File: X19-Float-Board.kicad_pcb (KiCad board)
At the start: 2 copper layers, 83.1 x 86.2 mm, 31 parts, among them J1 USB4220-03-1040-C_REVA, SW2 SW_Nidec_CAS-120A1, U3 STM32G431RBT6

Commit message: Checkpoint
Checkpoint, pre battery telemetry, pre new stm
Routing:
- net /Motor/Motor PWM: track 1.65 -> 45.1 mm, vias 0 -> 4
- net GND: track 200.7 -> 241.5 mm, vias 4 -> 6
- net VBUS_A: track 31.0 -> 38.1 mm, vias 5 -> 4
- net VBUS_B: track 3.12 -> 4.71 mm
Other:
- board text added: "yo"

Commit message: Update
Update
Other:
- board size 83.1 x 86.2 mm -> 86 x 86 mm

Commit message: todolist update
update of the to do list on schematic
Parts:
- added C_D_STM2: 100nF, Capacitor_SMD:C_0603_1608Metric, F.Cu at (177.0, 51.4)
- added C_D_STM3: 100nF, Capacitor_SMD:C_0603_1608Metric, F.Cu at (177.0, 53.9)
- added R_PD_USBC_1: 5.1k, Resistor_SMD:R_0603_1608Metric, F.Cu at (183.0, 51.4)
- added R_PD_USBC_2: 5.1kΩ, Resistor_SMD:R_0603_1608Metric, F.Cu at (183.0, 53.9)
- added R_USBC_DIV1: 20kΩ, Resistor_SMD:R_0603_1608Metric, F.Cu at (183.0, 56.4)
- added R_USBC_DIV2: 10kΩ, Resistor_SMD:R_0603_1608Metric, F.Cu at (183.0, 58.9)
- added U2: STM32C542CCT6, rov_logic:LQFP48-7X7, F.Cu at (169.2, 56.0)
- added U4: INA228AIDGSR, CustomFootprints:VSSOP10_DGS_TEX, F.Cu at (167.0, 66.2)
- added U5: TPS561208DDCR, CustomFootprints:DDC0006A_N, F.Cu at (175.6, 66.1)
- added U6: TMP1075NDRLR, CustomFootprints:SOT5X3-6_DRL_TEX, F.Cu at (165.7, 70.2)
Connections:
- DEPTH_CONN1 pad 2: /sensor/Depth SCL -> /Sensors/Depth SCL
- DEPTH_CONN1 pad 3: /sensor/Depth SDA -> /Sensors/Depth SDA
- R_PU_DEPTH_0 pad 1: /sensor/Depth SCL -> /Sensors/Depth SCL
- R_PU_DEPTH_1 pad 1: /sensor/Depth SDA -> /Sensors/Depth SDA

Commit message: footprints
footprints
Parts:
- removed BUCK_12_3.3: LM2596S-3.3, Package_TO_SOT_SMD:TO-263-5_TabPin3
- removed C_D_DEPTH1, C_D_MOTOR1, C_D_RF1, C_D_STM1, C_D_STM2, C_D_STM3, C_D_SWITCH1: 100nF, Capacitor_SMD:C_0603_1608Metric
- removed C_D_PWR_0: 680µF, Capacitor_SMD:C_0603_1608Metric
- removed C_D_PWR_1: 220µF, Capacitor_SMD:C_0603_1608Metric
- removed C_D_PWR_12, C_D_PWR_3.3: 4.7µF, Capacitor_SMD:C_0603_1608Metric
- removed D1: D_MOTOR, Diode_SMD:D_SOD-123
- removed DEPTH_CONN1: Conn_01x04_Pin, Connector_JST:JST_GH_BM04B-GHS-TBT_1x04-1MP_P1.25mm_Vertical
- removed D_PWR1: 1N5822, Diode_THT:D_DO-201AD_P15.24mm_Horizontal
- removed FUSE_PWR1: 2A 12V PTC fuse, Fuse:Fuse_1812_4532Metric
- removed J1: USB4220-03-1040-C_REVA, usbc:GCT_USB4220-03-1040-C_REVA
- removed L_PWR1: 33µH, Inductor_SMD:L_0603_1608Metric
- removed MOTOR_CONN1: Motor, TerminalBlock_Phoenix:TerminalBlock_Phoenix_MKDS-1,5-2-5.08_1x02_P5.08mm_Horizontal
- removed NMOS_MOTOR1: NMOS, Package_TO_SOT_SMD:SOT-23_Handsoldering
- removed R_PD_MOTOR1, R_PU_SWITCH1: 10kΩ, Resistor_SMD:R_0603_1608Metric
- removed R_PD_USBC_1 (x2): 5.1k, Resistor_SMD:R_0603_1608Metric
- removed R_PD_USBC_2 (x2): 5.1kΩ, Resistor_SMD:R_0603_1608Metric
- removed R_PU_DEPTH_0, R_PU_DEPTH_1: 4.7kΩ, Resistor_SMD:R_0603_1608Metric
- removed R_PWM_MOTOR1: 220Ω, Resistor_SMD:R_0603_1608Metric
- removed R_USBC_DIV0, R_USBC_DIV1: 20kΩ, Resistor_SMD:R_0603_1608Metric
- removed R_USBC_DIV1, R_USBC_DIV2: 10kΩ, Resistor_SMD:R_0603_1608Metric
- removed SCREW_PWR1: Screw_Terminal_01x02, TerminalBlock_Phoenix:TerminalBlock_Phoenix_MKDS-1,5-2-5.08_1x02_P5.08mm_Horizontal
- removed SW2: SW_Nidec_CAS-120A1, Button_Switch_SMD:Nidec_Copal_CAS-120A
- removed U1: ~, customrf:rf module
- removed U2: STM32C542CCT6, rov_logic:LQFP48-7X7
- removed U3: STM32G431RBT6, stm32:LQFP64-10x10mm
- removed U4: INA228AIDGSR, CustomFootprints:VSSOP10_DGS_TEX
- removed U5: TPS561208DDCR, CustomFootprints:DDC0006A_N
- removed U6: TMP1075NDRLR, CustomFootprints:SOT5X3-6_DRL_TEX
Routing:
- net GND: track 241.5 -> 0.00 mm, vias 6 -> 0
- net 3.3 V: track 149.3 -> 0.00 mm, vias 3 -> 0
- net 12 V: track 80.6 -> 0.00 mm, vias 2 -> 0
- net /rf/RF RST: track 45.4 -> 0.00 mm, vias 3 -> 0
- net /Motor/Motor PWM: track 45.1 -> 0.00 mm, vias 4 -> 0
- net /rf/RF NSS: track 45.0 -> 0.00 mm, vias 1 -> 0
- net /rf/RF MOSI: track 41.9 -> 0.00 mm, vias 3 -> 0
- net /sensor/Depth SDA: track 41.1 -> 0.00 mm
- net VBUS_A: track 38.1 -> 0.00 mm, vias 4 -> 0
- net /rf/RF MISO: track 37.4 -> 0.00 mm, vias 1 -> 0
- net /rf/RF SCK: track 36.4 -> 0.00 mm, vias 1 -> 0
- net /sensor/Depth SCL: track 33.5 -> 0.00 mm, vias 2 -> 0
- net /rf/RF INT: track 30.0 -> 0.00 mm, vias 1 -> 0
- net Net-(J1-DN2): track 23.7 -> 0.00 mm
- net Net-(D1-A): track 19.5 -> 0.00 mm, vias 1 -> 0
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- removed copper zone on F.Cu, net 12 V
- removed copper zone on F.Cu, net GND
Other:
- board text removed: "yo"

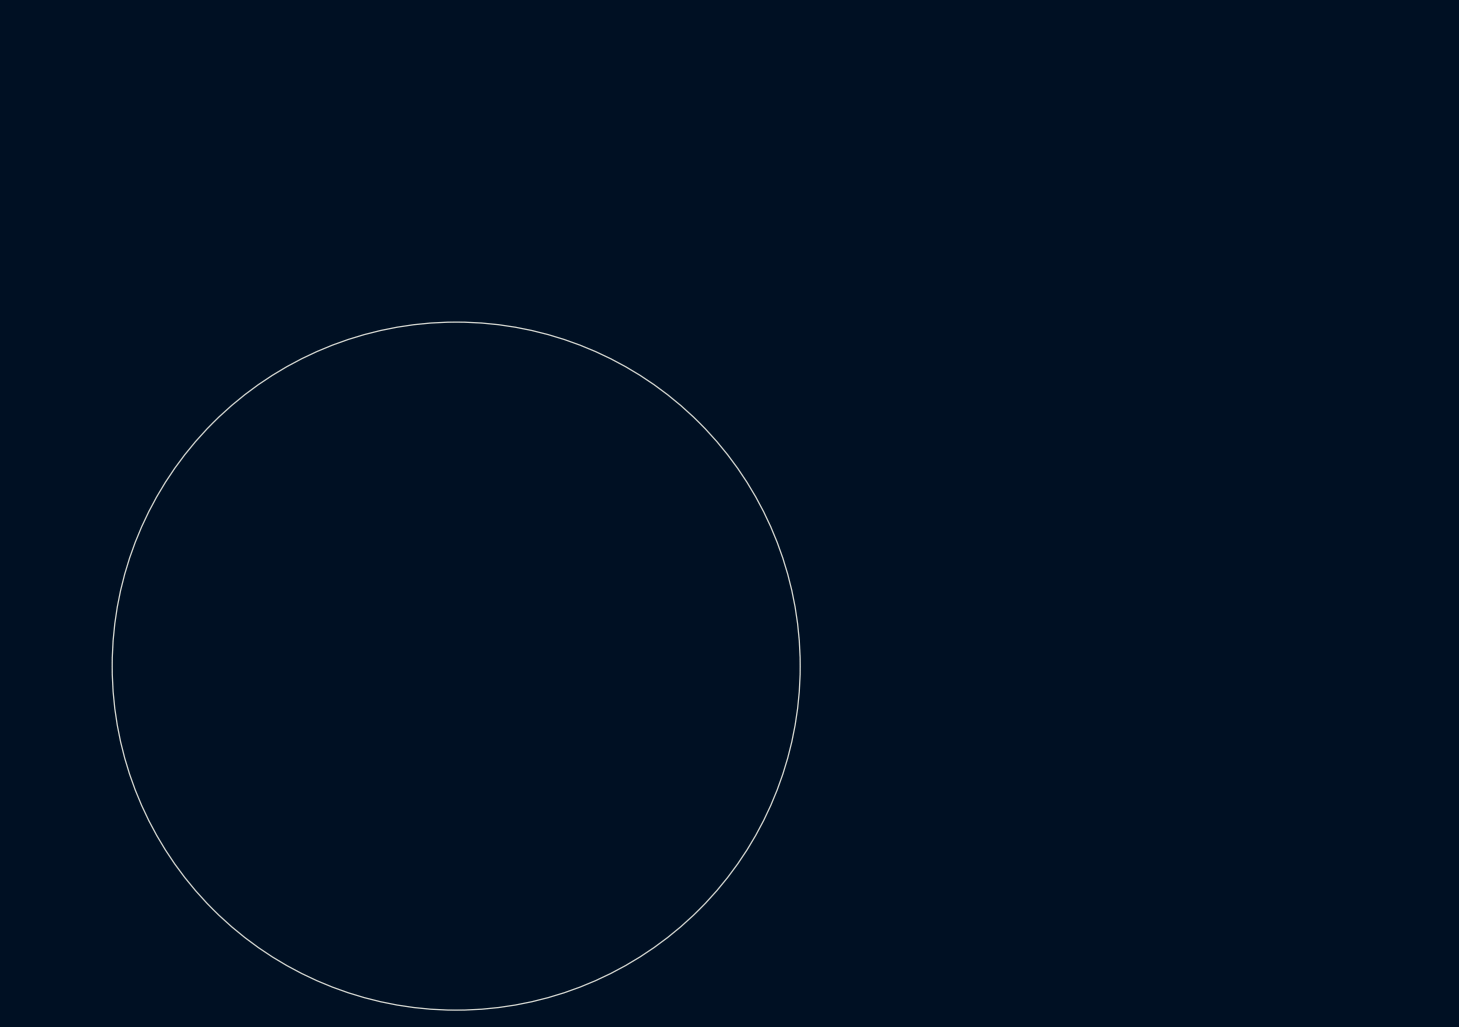
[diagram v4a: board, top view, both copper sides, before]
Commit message: Finished footprints
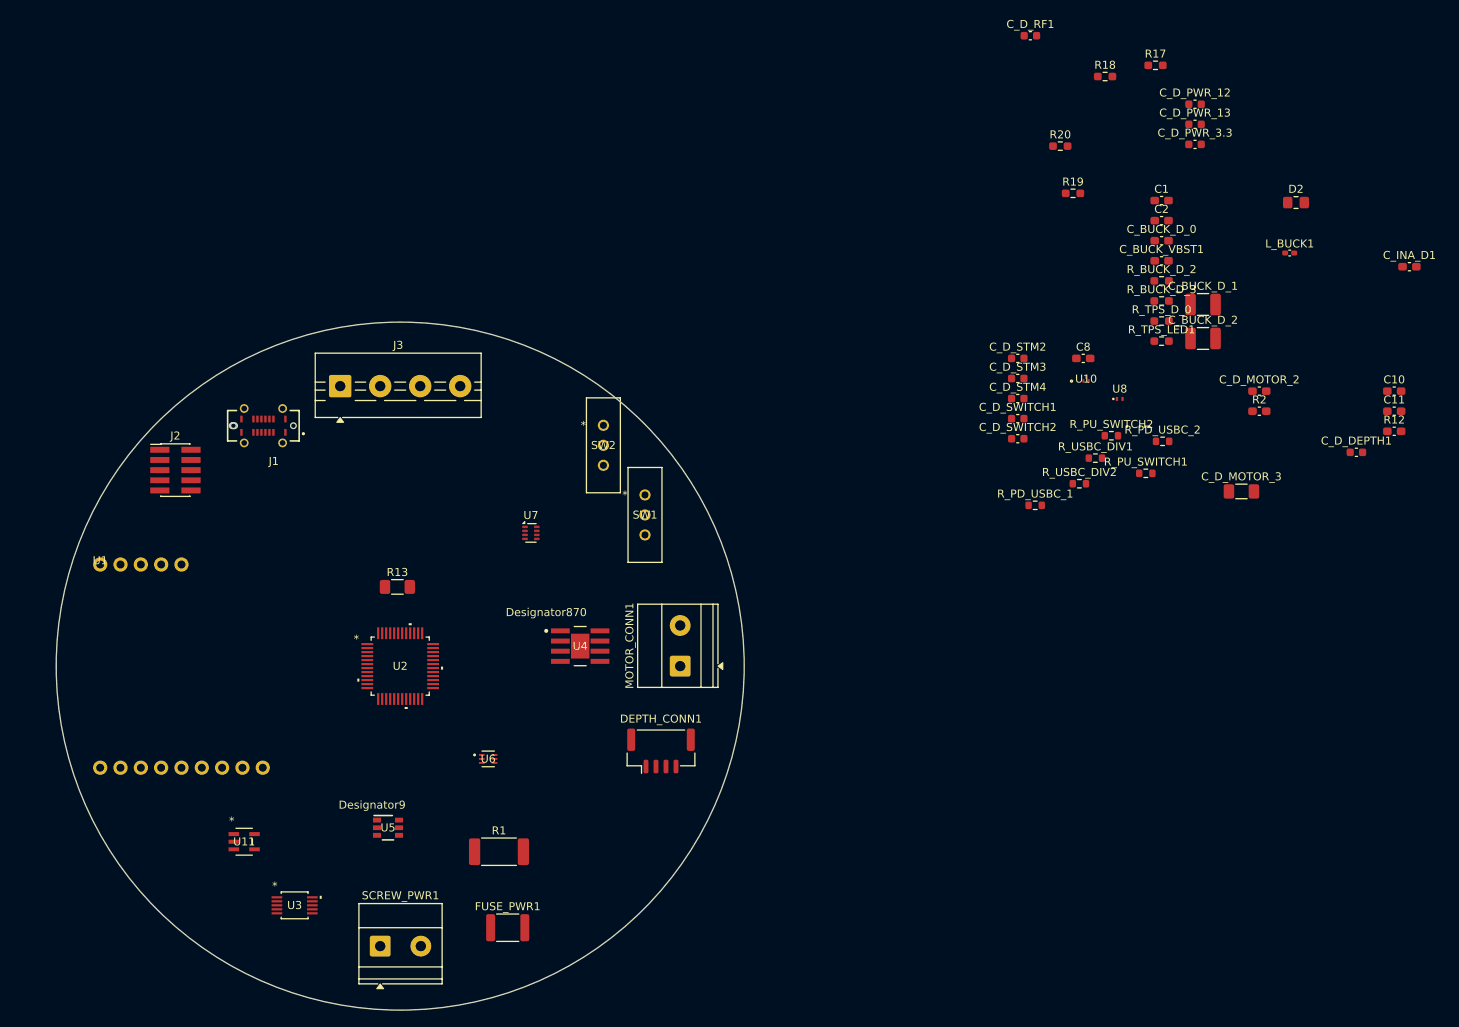
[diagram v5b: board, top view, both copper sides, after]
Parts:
- added C1: 1uF, Capacitor_SMD:C_0603_1608Metric_Pad1.08x0.95mm_HandSolder, F.Cu at (245.2, 41.8)
- added C10: 100nf, Capacitor_SMD:C_0603_1608Metric_Pad1.08x0.95mm_HandSolder, F.Cu at (274.3, 65.6)
- added C11: 10nf, Capacitor_SMD:C_0603_1608Metric_Pad1.08x0.95mm_HandSolder, F.Cu at (274.3, 68.1)
- added C2: 1uF, Capacitor_SMD:C_0603_1608Metric_Pad1.08x0.95mm_HandSolder, F.Cu at (245.2, 44.3)
- added C8: 100nf, Capacitor_SMD:C_0603_1608Metric_Pad1.08x0.95mm_HandSolder, F.Cu at (235.4, 61.5)
- added C_BUCK_D_0: .1uF, Capacitor_SMD:C_0603_1608Metric_Pad1.08x0.95mm_HandSolder, F.Cu at (245.2, 46.8)
- added C_BUCK_D_1: 22uF, Capacitor_SMD:C_1210_3225Metric_Pad1.33x2.70mm_HandSolder, F.Cu at (250.4, 54.8)
- added C_BUCK_D_2: 22uF, Capacitor_SMD:C_1210_3225Metric_Pad1.33x2.70mm_HandSolder, F.Cu at (250.4, 59.0)
- added C_BUCK_VBST1: 0.1 uF, Capacitor_SMD:C_0603_1608Metric_Pad1.08x0.95mm_HandSolder, F.Cu at (245.2, 49.3)
- added C_D_DEPTH1: 100nF, Capacitor_SMD:C_0603_1608Metric, F.Cu at (269.5, 73.3)
- added C_D_MOTOR_2: 10uf, Capacitor_SMD:C_0603_1608Metric_Pad1.08x0.95mm_HandSolder, F.Cu at (257.4, 65.6)
- added C_D_MOTOR_3: 47uf, Capacitor_SMD:C_1206_3216Metric_Pad1.33x1.80mm_HandSolder, F.Cu at (255.2, 78.2)
- added C_D_PWR_12: 4.7µF, Capacitor_SMD:C_0603_1608Metric, F.Cu at (249.4, 29.8)
- added C_D_PWR_13: 4.7µF, Capacitor_SMD:C_0603_1608Metric, F.Cu at (249.4, 32.3)
- added C_D_PWR_3.3: 4.7µF, Capacitor_SMD:C_0603_1608Metric, F.Cu at (249.4, 34.8)
- added C_D_RF1: 100nF, Capacitor_SMD:C_0603_1608Metric, F.Cu at (228.8, 21.2)
- added C_D_STM2: 100nF, Capacitor_SMD:C_0603_1608Metric, F.Cu at (227.2, 61.5)
- added C_D_STM3: 100nF, Capacitor_SMD:C_0603_1608Metric, F.Cu at (227.2, 64.0)
- added C_D_STM4: 2.2uF, Capacitor_SMD:C_0603_1608Metric, F.Cu at (227.2, 66.6)
- added C_D_SWITCH1: 100nF, Capacitor_SMD:C_0603_1608Metric, F.Cu at (227.2, 69.1)
- added C_D_SWITCH2: 100nF, Capacitor_SMD:C_0603_1608Metric, F.Cu at (227.2, 71.6)
- added C_INA_D1: 100nf, Capacitor_SMD:C_0603_1608Metric_Pad1.08x0.95mm_HandSolder, F.Cu at (276.2, 50.1)
- added D2: PWR Indicator, Capacitor_SMD:C_0805_2012Metric_Pad1.18x1.45mm_HandSolder, F.Cu at (262.0, 42.1)
- added DEPTH_CONN1: 01x04, Connector_JST:JST_GH_BM04B-GHS-TBT_1x04-1MP_P1.25mm_Vertical, F.Cu at (182.6, 110.6)
- added FUSE_PWR1: 2A 12V PTC fuse, Fuse:Fuse_1812_4532Metric, F.Cu at (163.4, 132.7)
- added J1: USB4220-03-1040-C_REVA, CustomFootprints:GCT_USB4220-03-1040-C_REVA, F.Cu at (132.9, 70.0)
- added J2: STLINK Connector, Connector_PinHeader_1.27mm:PinHeader_2x05_P1.27mm_Vertical_SMD, F.Cu at (121.9, 75.5)
- added J3: SZ conn, TerminalBlock:TerminalBlock_MaiXu_MX126-5.0-04P_1x04_P5.00mm, F.Cu at (142.5, 65.0)
- added L_BUCK1: 3.3uH, Capacitor_SMD:C_0402_1005Metric_Pad0.74x0.62mm_HandSolder, F.Cu at (261.2, 48.4)
- added MOTOR_CONN1: MOTOR_CONN2, TerminalBlock_Phoenix:TerminalBlock_Phoenix_MKDS-1,5-2-5.08_1x02_P5.08mm_Horizontal, F.Cu at (185.0, 100.0)
- added R1: 1 mΩ, Resistor_SMD:R_2512_6332Metric_Pad1.40x3.35mm_HandSolder, F.Cu at (162.3, 123.2)
- added R12: 10k, Capacitor_SMD:C_0603_1608Metric_Pad1.08x0.95mm_HandSolder, F.Cu at (274.3, 70.6)
- added R13: Generic Photoresistor, Resistor_SMD:R_1206_3216Metric_Pad1.30x1.75mm_HandSolder, F.Cu at (149.7, 90.1)
- added R17: 10k, Resistor_SMD:R_0603_1608Metric_Pad0.98x0.95mm_HandSolder, F.Cu at (244.4, 24.9)
- added R18: 10k, Resistor_SMD:R_0603_1608Metric_Pad0.98x0.95mm_HandSolder, F.Cu at (238.1, 26.3)
- added R19: 10k, Resistor_SMD:R_0603_1608Metric_Pad0.98x0.95mm_HandSolder, F.Cu at (234.1, 40.9)
- added R2: 10k, Capacitor_SMD:C_0603_1608Metric_Pad1.08x0.95mm_HandSolder, F.Cu at (257.4, 68.1)
- added R20: 10k, Resistor_SMD:R_0603_1608Metric_Pad0.98x0.95mm_HandSolder, F.Cu at (232.5, 35.0)
- added R_BUCK_D_2: 10k, Resistor_SMD:R_0603_1608Metric_Pad0.98x0.95mm_HandSolder, F.Cu at (245.2, 51.8)
- added R_BUCK_D_3: 33.2k, Resistor_SMD:R_0603_1608Metric_Pad0.98x0.95mm_HandSolder, F.Cu at (245.2, 54.4)
- added R_PD_USBC_1: 5.1k, Resistor_SMD:R_0603_1608Metric, F.Cu at (229.4, 79.9)
- added R_PD_USBC_2: 5.1kΩ, Resistor_SMD:R_0603_1608Metric, F.Cu at (245.3, 71.9)
- added R_PU_SWITCH1: 10kΩ, Resistor_SMD:R_0603_1608Metric, F.Cu at (243.2, 75.9)
- added R_PU_SWITCH2: 10kΩ, Resistor_SMD:R_0603_1608Metric, F.Cu at (238.9, 71.2)
- added R_TPS_D_0: 15k, Resistor_SMD:R_0603_1608Metric_Pad0.98x0.95mm_HandSolder, F.Cu at (245.2, 56.9)
- added R_TPS_LED1: 1k, Resistor_SMD:R_0603_1608Metric_Pad0.98x0.95mm_HandSolder, F.Cu at (245.2, 59.4)
- added R_USBC_DIV1: 20kΩ, Resistor_SMD:R_0603_1608Metric, F.Cu at (236.9, 74.0)
- added R_USBC_DIV2: 10kΩ, Resistor_SMD:R_0603_1608Metric, F.Cu at (234.9, 77.2)
- added SCREW_PWR1: 01x02, TerminalBlock_Phoenix:TerminalBlock_Phoenix_MKDS-1,5-2-5.08_1x02_P5.08mm_Horizontal, F.Cu at (147.5, 135.0)
- added SW1: EG1218, CustomFootprints:EG_1218_EWI, F.Cu at (180.6, 78.6)
- added SW2: EG1218, CustomFootprints:EG_1218_EWI, F.Cu at (175.4, 69.9)
- added U1: ~, CustomFootprints:rf module, F.Cu at (112.5, 87.3)
- added U10: ESD122DMXR, CustomFootprints:DMX3_TEX, F.Cu at (235.7, 64.1)
- added U11: MIC5504-3.3YM5-TR, rov_power:SOT-23-5_MC_MCH, F.Cu at (130.5, 121.9)
- added U2: STM32C542CCT6, rov_logic:LQFP48-7X7, F.Cu at (150.0, 100.0)
- added U3: INA237AIDGSR, rov_sensors:VSSOP_IDGSR_TEX, F.Cu at (136.8, 129.9)
- added U4: DRV8231DDAR, CustomFootprints:DDA0008J-IPC_A, F.Cu at (172.5, 97.5)
- added U5: TPS561208DDCR, CustomFootprints:DDC0006A_N, F.Cu at (148.5, 120.2)
- added U6: TMP1075NDRLR, CustomFootprints:SOT5X3-6_DRL_TEX, F.Cu at (161.0, 111.6)
- added U7: TPS2116DRL, Package_TO_SOT_SMD:SOT-583-8, F.Cu at (166.3, 83.3)
- added U8: TPD1E05U06DPY, Package_SON:Texas_DPY0002A_0.6x1mm_P0.65mm, F.Cu at (239.9, 66.6)
